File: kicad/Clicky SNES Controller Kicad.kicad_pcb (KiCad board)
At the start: 2 copper layers, 41.9 x 44.8 mm, 39 parts, among them CN1 CN1, P11 TL_IN, P13 TR_IN, P2 VSS_Trigger, P3 TR_TL_OUT, P4 DPAD_IN, P6 ABXY_IN, U1 4021, U2 4021, X1 SW_PUSH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

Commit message: PCB: Route back side of board
This is the simpler side of the board, but getting a basic layout
in place will help when routing the top side as I will know where
I can drop a via through to jump over other tracks.
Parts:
- moved R17 6.76 mm to (53.1, 48.8), turned to 270 degrees
- moved C1 6.67 mm to (53.1, 42.1), turned to 270 degrees
- moved R1 4.11 mm to (33.4, 29.5), turned to 90 degrees
- turned R7 to 0 degrees
- turned R8 to 0 degrees
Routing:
- net GND: track 0.00 -> 72.5 mm
- net /A_switch: track 0.00 -> 29.8 mm
- net /B_switch: track 0.00 -> 26.0 mm
- net +5V: track 0.00 -> 25.3 mm
- net /Left: track 0.00 -> 19.3 mm, vias 0 -> 1
- net /DLATCH: track 0.00 -> 10.1 mm
- net Net-(P3-Pad1): track 0.00 -> 8.38 mm
- net /VSS_Trigger: track 0.00 -> 5.20 mm
- net /DCLK: track 0.00 -> 2.81 mm
- net /Right: track 0.00 -> 1.69 mm
- added copper zone on B.Cu, net GND

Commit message: PCB: Minor optimization for back-side
Noticed a missing GND route.
Moved the DLATCH pullup resistor in order to facilitate some better
pathing for the A_switch and GND nets.
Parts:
- moved R2 6.48 mm to (35.4, 23.3)
- moved R1 0.20 mm to (33.4, 29.7)
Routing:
- net GND: track 72.5 -> 83.3 mm
- net +5V: track 25.3 -> 27.9 mm
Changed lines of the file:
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@@
     (thickness 1.6)
     (drawings 194)
-    (tracks 71)
+    (tracks 78)
     (zones 0)
     (modules 39)
@@
   )
   (layers
-    (0 F.Cu signal hide)
+    (0 F.Cu signal)
     (31 B.Cu signal)
     (32 B.Adhes user hide)
@@
     (39 F.Mask user)
     (40 Dwgs.User user)
-    (41 Cmts.User user hide)
+    (41 Cmts.User user)
     (42 Eco1.User user hide)
     (43 Eco2.User user hide)
@@
     (pad_to_paste_clearance -0.04)
     (aux_axis_origin 0 0)
-    (visible_elements 7FFEB77F)
+    (visible_elements 7FFEF77F)
     (pcbplotparams
       (layerselection 0x3ffff_80000001)
@@
   )
   (module Resistors_SMD:R_1206_HandSoldering (layer B.Cu)
-    (at 33.4 29.5 90)
+    (at 33.4 29.7 90)
     (descr "Resistor SMD 1206, hand soldering")
     (tags "resistor 1206")
@@
   )
   (module Resistors_SMD:R_1206_HandSoldering (layer B.Cu)
-    (at 40.386 27.432 180)
+    (at 35.4 23.3 180)
     (descr "Resistor SMD 1206, hand soldering")
     (tags "resistor 1206")
@@
   (gr_line (start 12.718048 22.641765) (end 12.718048 49.698535) (layer Eco1.User) (width 0.1))
   (gr_line (start 13.614557 21.399534) (end 12.718048 22.641765) (layer Eco1.User) (width 0.1))
-  (segment (start 35.687 27.686) (end 33.586 27.686) (width 1.7) (layer B.Cu) (net 2))
-  (segment (start 33.586 27.686) (end 33.4 27.5) (width 1.7) (layer B.Cu) (net 2))
+  (segment (start 33.4 27.7) (end 33.4 23.3) (width 1.7) (layer B.Cu) (net 2))
+  (segment (start 34.7 27.686) (end 33.586 27.686) (width 1.7) (layer B.Cu) (net 2))
+  (segment (start 35.687 27.686) (end 34.7 27.686) (width 1.7) (layer B.Cu) (net 2))
+  (segment (start 34.7 27.686) (end 33.414 27.686) (width 1.7) (layer B.Cu) (net 2))
+  (segment (start 33.414 27.686) (end 33.4 27.7) (width 1.7) (layer B.Cu) (net 2))
   (segment (start 28.797 55.88) (end 28.797 53.594) (width 1.7) (layer F.Cu) (net 2))
   (segment (start 40.64 55.594) (end 38.481 55.594) (width 1.7) (layer F.Cu) (net 2))
@@
   (segment (start 17.526 42.386) (end 16.637 41.497) (width 1.7) (layer F.Cu) (net 2))
   (segment (start 53.1175 55.753) (end 53.1175 53.34) (width 1.7) (layer F.Cu) (net 2))
-  (segment (start 38.386 27.432) (end 35.941 27.432) (width 1.7) (layer B.Cu) (net 2))
-  (segment (start 35.941 27.432) (end 35.687 27.686) (width 1.7) (layer B.Cu) (net 2))
+  (segment (start 39.375 29.432) (end 41.505 29.432) (width 0.58) (layer B.Cu) (net 3))
+  (segment (start 41.505 29.432) (end 42.956401 30.883401) (width 0.58) (layer B.Cu) (net 3))
+  (segment (start 42.956401 30.883401) (end 46.713599 30.883401) (width 0.58) (layer B.Cu) (net 3))
+  (segment (start 46.713599 30.883401) (end 48.006 29.591) (width 0.58) (layer B.Cu) (net 3))
+  (segment (start 44.86 39.719) (end 43.81 39.719) (width 0.58) (layer B.Cu) (net 3))
+  (segment (start 53.34 29.21) (end 48.387 29.21) (width 0.58) (layer B.Cu) (net 3))
+  (segment (start 48.387 29.21) (end 48.006 29.591) (width 0.58) (layer B.Cu) (net 3))
   (segment (start 25.786 39.846) (end 25.786 38.766) (width 0.58) (layer B.Cu) (net 3))
   (segment (start 25.786 38.766) (end 23.370999 36.350999) (width 0.58) (layer B.Cu) (net 3))
@@
   (segment (start 30.475 29.432) (end 24.924 29.432) (width 0.58) (layer B.Cu) (net 3))
   (segment (start 24.924 29.432) (end 24.765 29.591) (width 0.58) (layer B.Cu) (net 3))
-  (segment (start 48.006 29.591) (end 48.387 29.21) (width 1) (layer B.Cu) (net 3))
-  (segment (start 48.387 29.21) (end 53.34 29.21) (width 1) (layer B.Cu) (net 3))
   (segment (start 30.348 46.26) (end 30.348 44.5786) (width 0.58) (layer B.Cu) (net 3))
   (segment (start 30.348 44.5786) (end 31.888 43.0386) (width 0.58) (layer B.Cu) (net 3))
@@
   (segment (start 50.673 30.353) (end 53.34 33.02) (width 0.35) (layer F.Cu) (net 4))
   (via (at 39.375 25.432) (size 0.6858) (drill 0.3302) (layers F.Cu B.Cu) (net 4))
-  (segment (start 42.386 27.432) (end 42.386 29.450202) (width 0.58) (layer B.Cu) (net 5))
-  (segment (start 42.386 29.450202) (end 39.070202 32.766) (width 0.58) (layer B.Cu) (net 5))
-  (segment (start 39.070202 32.766) (end 36.889081 32.766) (width 0.58) (layer B.Cu) (net 5))
-  (segment (start 36.889081 32.766) (end 35.687 32.766) (width 0.58) (layer B.Cu) (net 5))
+  (segment (start 35.687 32.766) (end 37.2 31.253) (width 0.58) (layer B.Cu) (net 5))
+  (segment (start 37.2 31.253) (end 37.2 23.5) (width 0.58) (layer B.Cu) (net 5))
+  (segment (start 37.2 23.5) (end 37.4 23.3) (width 0.58) (layer B.Cu) (net 5))
   (segment (start 178.6686 25.813) (end 178.6816 25.8) (width 1) (layer F.Cu) (net 7))
   (segment (start 178.6816 25.8) (end 182.9372 25.8) (width 1) (layer F.Cu) (net 7))
@@
   (segment (start 53.34 34.29) (end 53.34 35.089) (width 1) (layer B.Cu) (net 14))
   (segment (start 53.34 35.089) (end 52.71 35.719) (width 1) (layer B.Cu) (net 14))
+  (segment (start 46.6 32.8) (end 51.02 32.8) (width 0.35) (layer B.Cu) (net 21))
+  (segment (start 51.02 32.8) (end 53.34 30.48) (width 0.35) (layer B.Cu) (net 21))
+  (segment (start 45.456599 33.943401) (end 46.6 32.8) (width 0.35) (layer B.Cu) (net 21))
   (segment (start 25.786 35.846) (end 27.686 35.846) (width 0.35) (layer B.Cu) (net 21))
   (segment (start 27.686 35.846) (end 29.588599 33.943401) (width 0.35) (layer B.Cu) (net 21))
-  (segment (start 29.588599 33.943401) (end 49.876599 33.943401) (width 0.35) (layer B.Cu) (net 21))
-  (segment (start 49.876599 33.943401) (end 52.840001 30.979999) (width 0.35) (layer B.Cu) (net 21))
-  (segment (start 52.840001 30.979999) (end 53.34 30.48) (width 0.35) (layer B.Cu) (net 21))
+  (segment (start 29.588599 33.943401) (end 45.456599 33.943401) (width 0.35) (layer B.Cu) (net 21))
   (segment (start 39.248 50.26) (end 42.054804 50.26) (width 0.35) (layer B.Cu) (net 22))
   (segment (start 42.054804 50.26) (end 50.832599 41.482205) (width 0.35) (layer B.Cu) (net 22))
@@
   (segment (start 50.832599 34.257401) (end 52.840001 32.249999) (width 0.35) (layer B.Cu) (net 22))
   (segment (start 52.840001 32.249999) (end 53.34 31.75) (width 0.35) (layer B.Cu) (net 22))
-  (segment (start 33.4 31.5) (end 34.413 31.5) (width 0.58) (layer B.Cu) (net 23))
-  (segment (start 34.413 31.5) (end 35.687 30.226) (width 0.58) (layer B.Cu) (net 23))
+  (segment (start 33.4 31.7) (end 33.4 31.8) (width 0.58) (layer B.Cu) (net 23))
+  (segment (start 33.4 31.8) (end 34.113 31.8) (width 0.58) (layer B.Cu) (net 23))
+  (segment (start 34.113 31.8) (end 35.687 30.226) (width 0.58) (layer B.Cu) (net 23))
   (zone (net 3) (net_name GND) (layer B.Cu) (hatch edge 0.508)
     (connect_pads yes (clearance 0.1524))

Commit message: PCB: Add power tracks to top layer
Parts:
- C1: moved to B.Cu
- moved C1 10.2 mm to (48.7, 51.3), turned to 180 degrees
- moved R16 2.42 mm to (51.1, 55.8)
- moved R15 2.40 mm to (51.1, 53.4)
- moved R18 2.29 mm to (36.7, 46.5)
- moved R13 2.14 mm to (38.5, 53.6)
- moved R14 2.12 mm to (40.6, 53.6)
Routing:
- net +5V: track 27.9 -> 132.1 mm, vias 0 -> 3
- net GND: track 83.3 -> 152.9 mm, vias 0 -> 3
- net /Start: track 0.00 -> 30.4 mm, vias 0 -> 1
- net /Select: track 0.00 -> 16.1 mm, vias 0 -> 1
- net /B_switch: track 26.0 -> 37.5 mm
- net /A_switch: track 29.8 -> 39.2 mm
- net /Right: track 1.69 -> 8.86 mm
- net /B: track 0.00 -> 7.15 mm
- net /Left: track 19.3 -> 25.6 mm

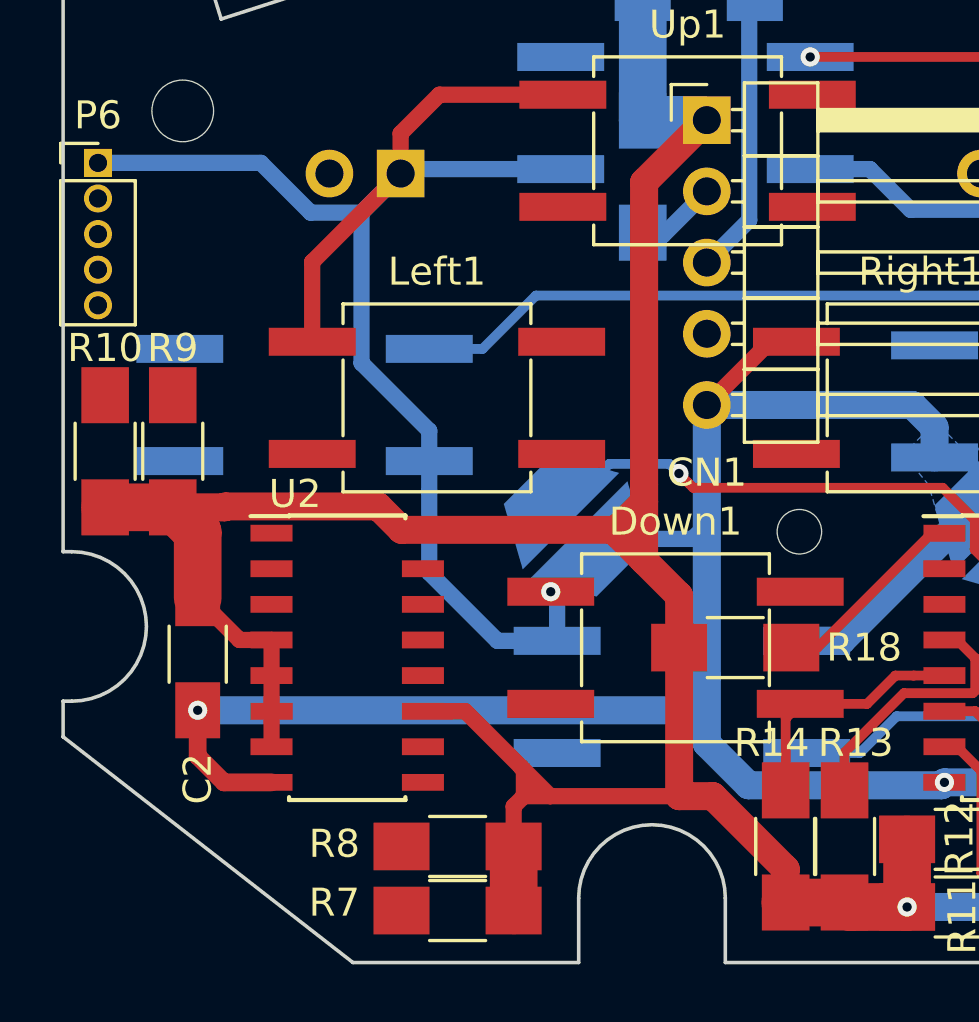
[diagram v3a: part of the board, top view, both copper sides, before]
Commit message: PCB: Move C2 to reduce GND loop area with U2
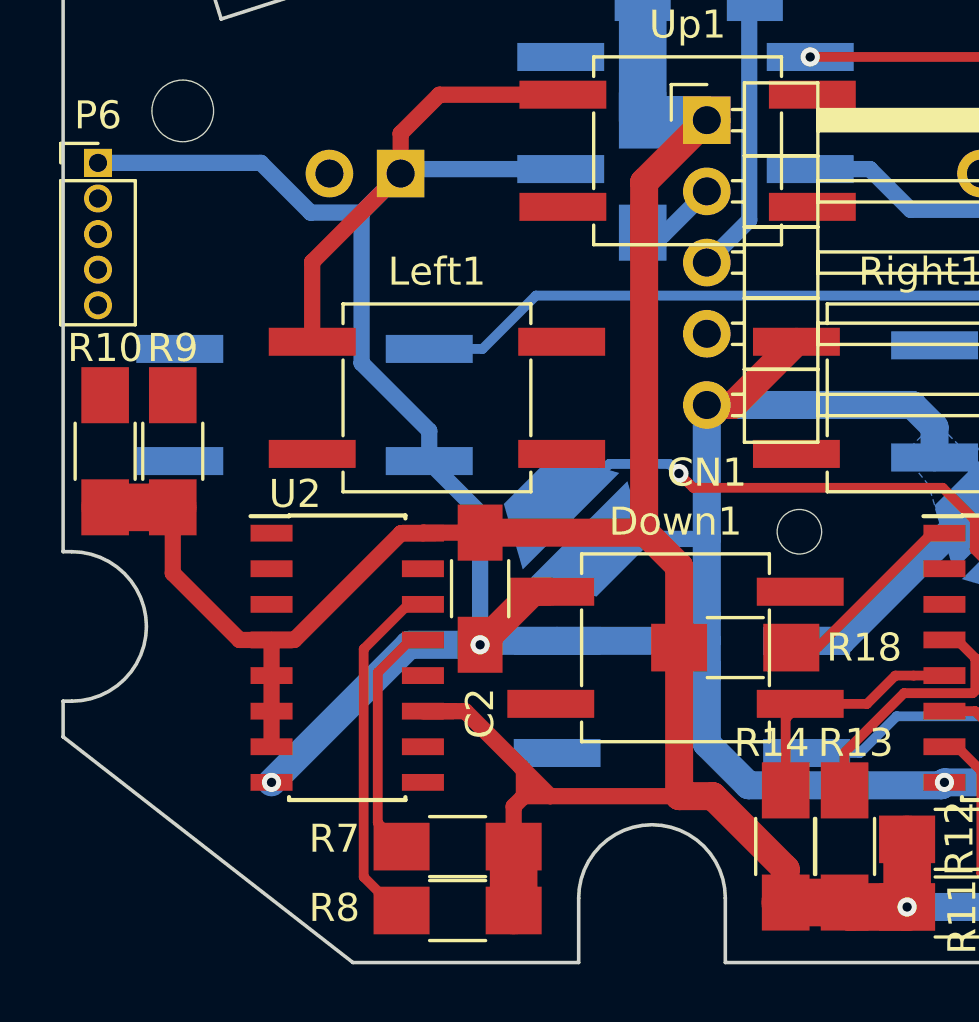
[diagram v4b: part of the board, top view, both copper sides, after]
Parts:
- moved C2 10.3 mm to (27.6, 44.4)
- moved R8 2.29 mm to (26.8, 55.9)
- moved R7 2.28 mm to (26.8, 53.6)
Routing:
- net /TL: track 0.00 -> 12.7 mm
- net /TR: track 0.00 -> 8.65 mm
- net +5V: track 132.1 -> 123.7 mm
- net GND: track 152.9 -> 146.8 mm

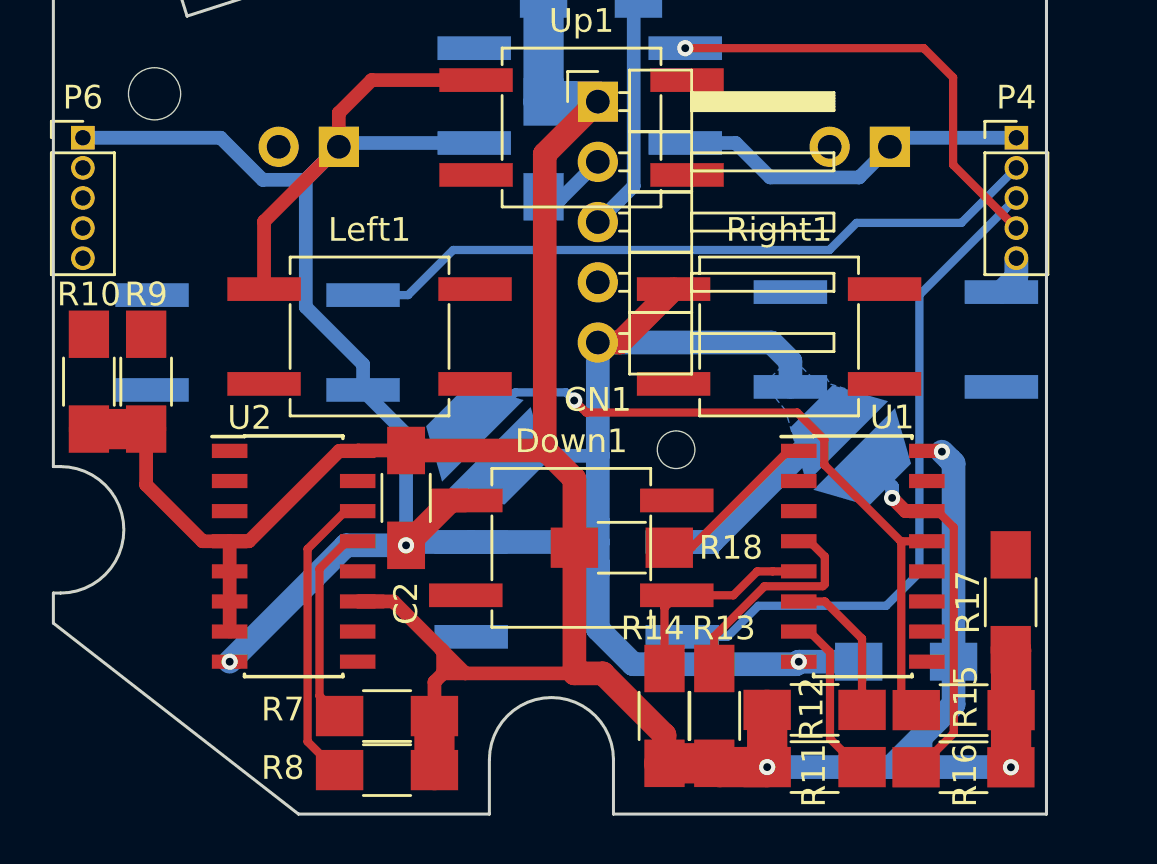
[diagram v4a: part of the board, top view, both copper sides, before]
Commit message: PCB: Finish routing passives
Had to fuss with the +5V route and placement of some of the
resistors to get this to work out reasonably well.
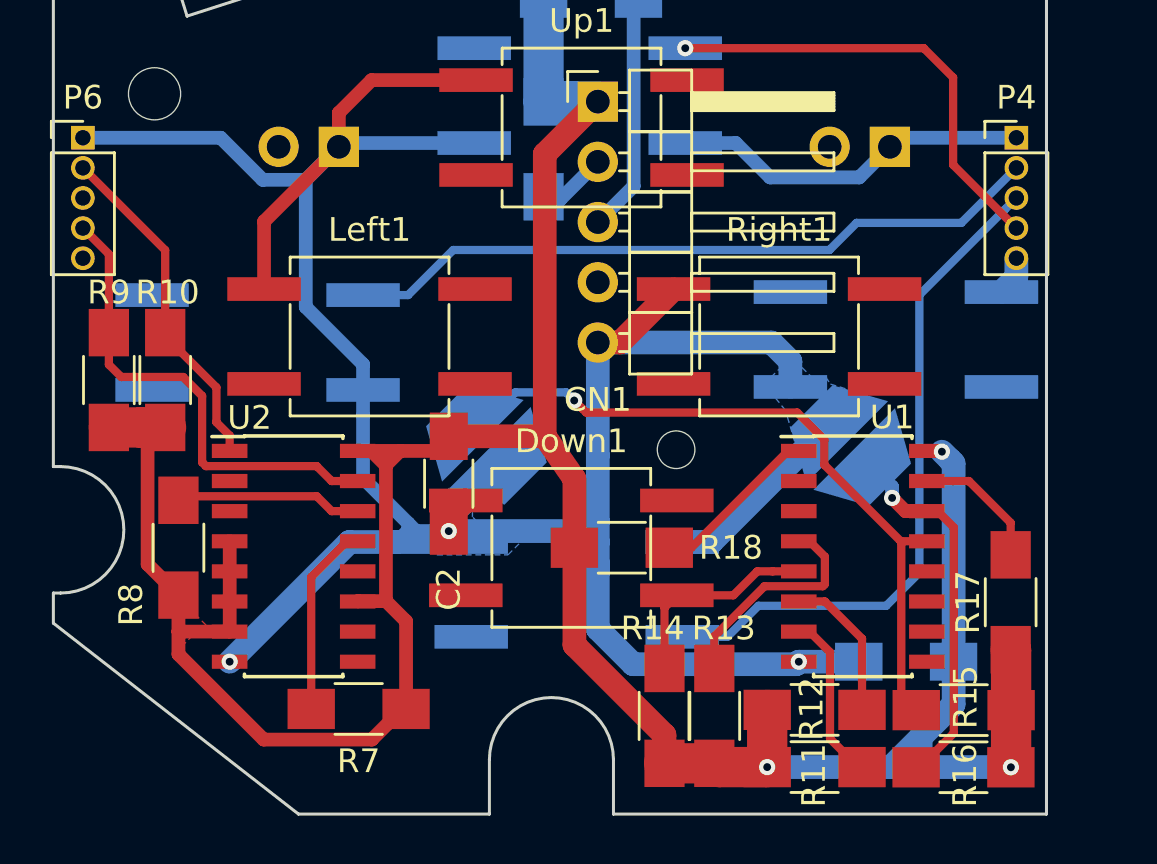
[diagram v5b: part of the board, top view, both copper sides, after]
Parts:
- moved R8 12.9 mm to (18.0, 46.5), turned to 270 degrees
- moved R10 3.22 mm to (17.4, 39.4)
- moved C2 1.90 mm to (29.4, 43.8)
- moved R9 1.57 mm to (15.1, 39.4)
- moved R7 1.23 mm to (25.6, 53.3)
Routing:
- net /X: track 0.00 -> 20.4 mm
- net /A: track 0.00 -> 14.7 mm
- net +5V: track 123.7 -> 129.7 mm
- net /Y: track 0.00 -> 5.62 mm
- net /TL: track 12.7 -> 7.89 mm
- net GND: track 146.8 -> 145.9 mm
- net /TR: track 8.65 -> 8.15 mm
- added copper zone on F.Cu, net +5V

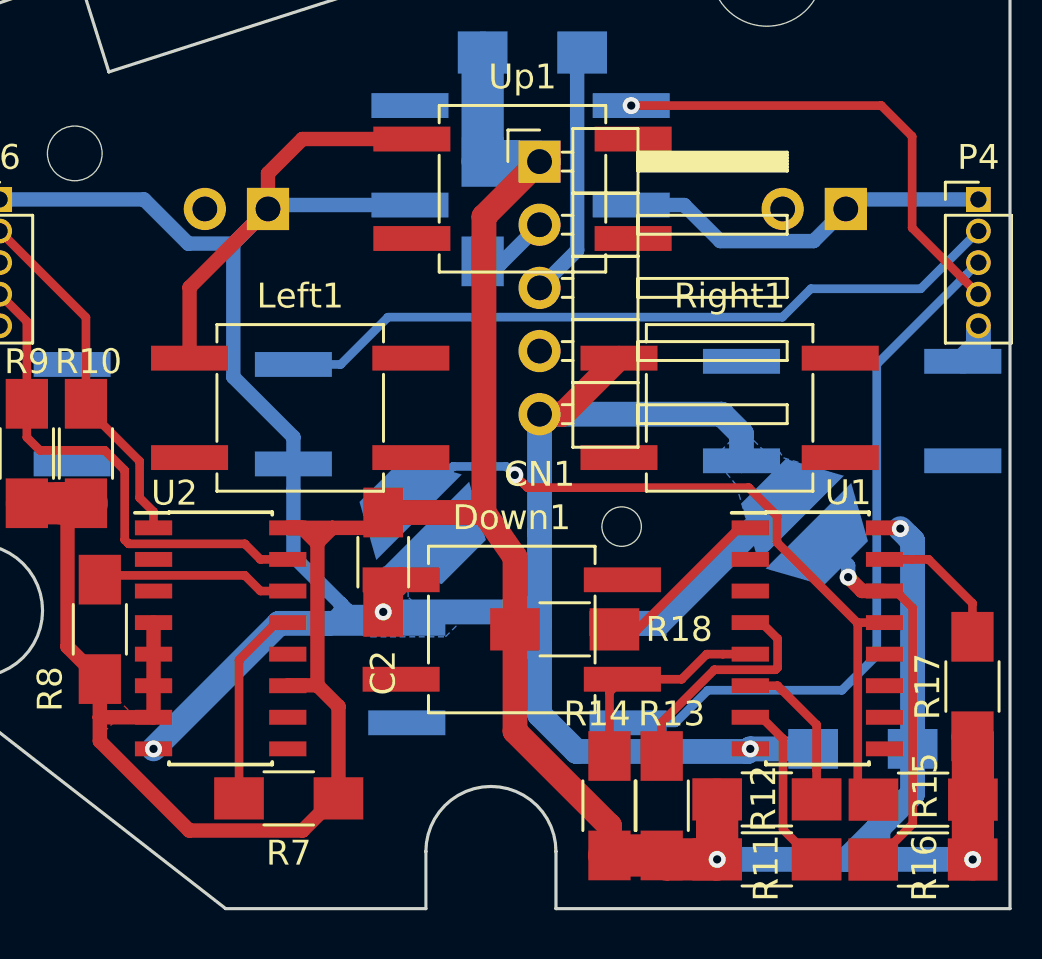
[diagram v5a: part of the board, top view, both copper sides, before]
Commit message: PCB: Route remaining Clock, Latch, and Serout nets
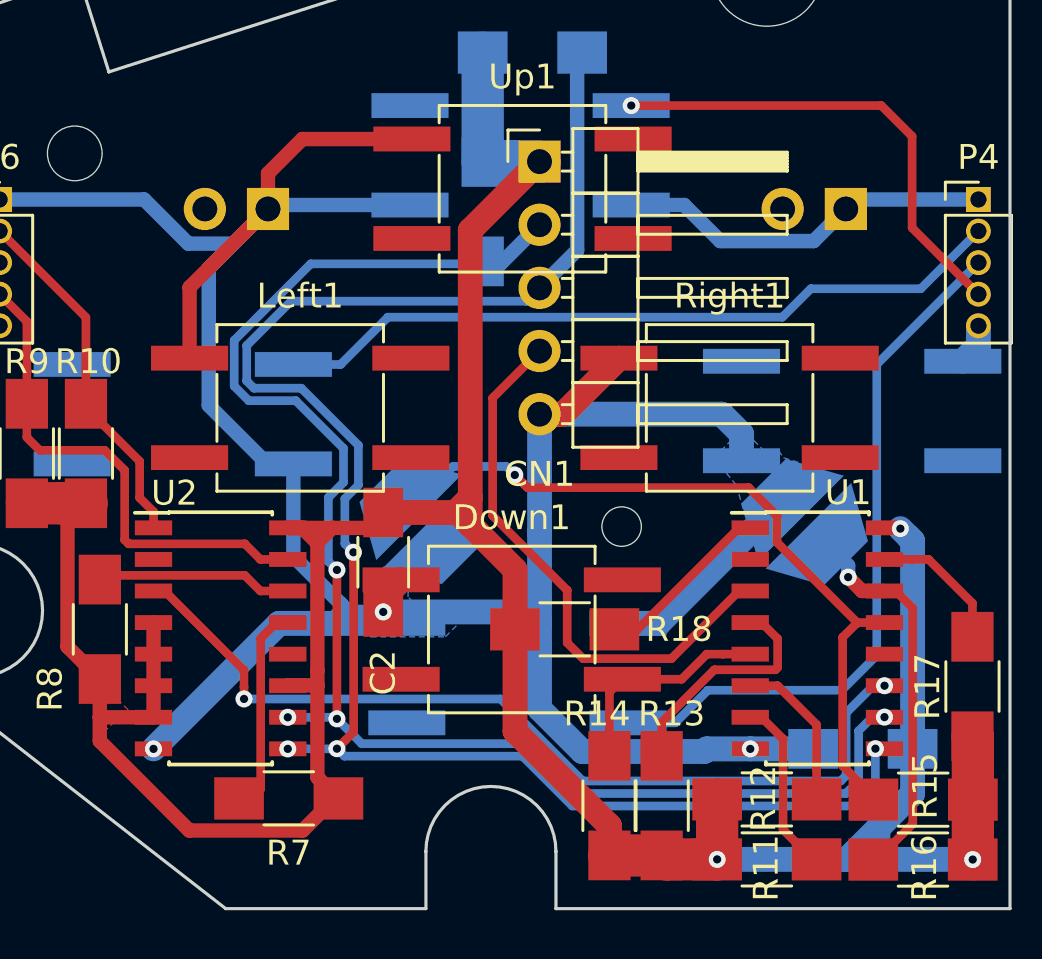
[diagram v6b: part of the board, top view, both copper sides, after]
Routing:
- net /DLATCH: track 10.2 -> 69.1 mm, vias 0 -> 4
- net /DCLK: track 3.04 -> 60.6 mm, vias 0 -> 4
- net Net-(U1-Pad11): track 0.00 -> 36.3 mm, vias 0 -> 2
- net /SEROUT: track 0.00 -> 22.5 mm
- net GND: track 145.9 -> 147.2 mm
- net +5V: track 129.7 -> 130.8 mm
- net /Start: track 30.4 -> 30.9 mm
